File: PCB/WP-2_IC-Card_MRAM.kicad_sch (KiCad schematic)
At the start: 31 parts, among them J1 SMS-138-01-G-S, SW1 CUS-14TB, U1 MRxA08xxYSxxx, U2 MIC5317-3.3YD5, U3 4245, U4 4245, U5 4245, U6 4245

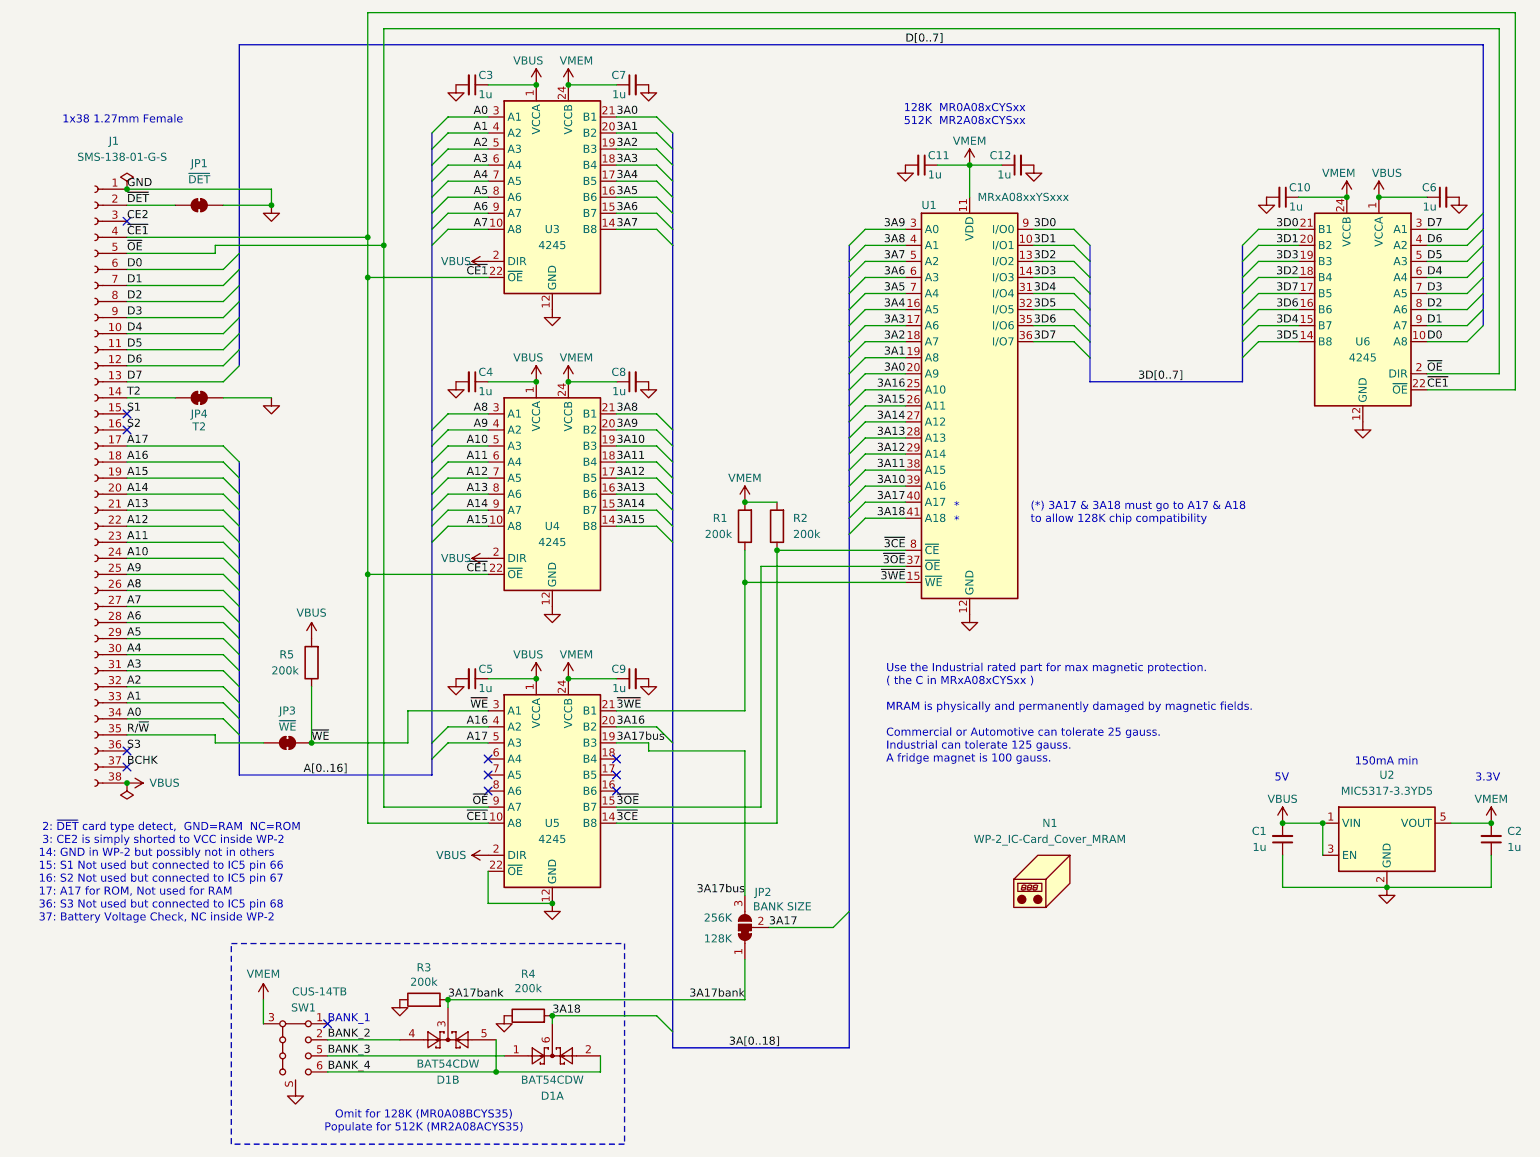
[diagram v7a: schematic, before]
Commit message: mram bav74 diodes
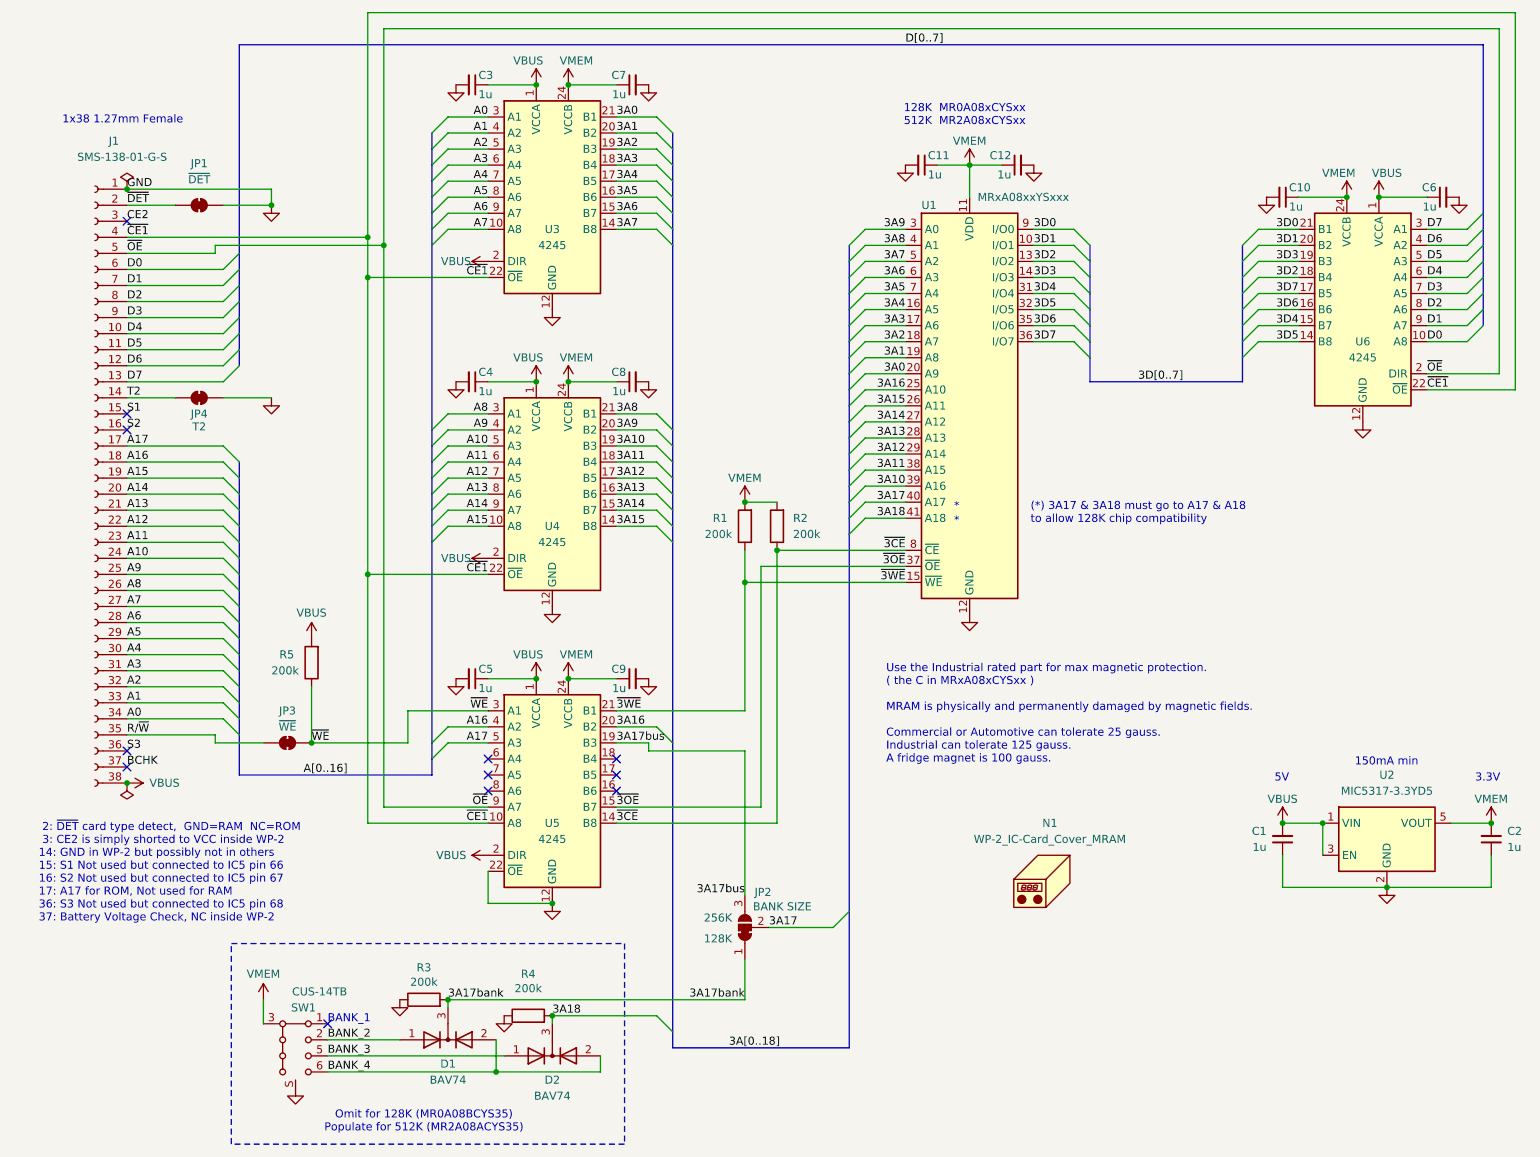
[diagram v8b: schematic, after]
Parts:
- removed D1: BAT54CDW, 000_LOCAL:TSSOP-6-symmetric, symbol 000_LOCAL:BAT54CDW
- added D1, D2: BAV74, 000_LOCAL:SOT-23, symbol 000_LOCAL:BAV170
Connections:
- net 3A17bank: now also D1.3 (K)
- net 3A18: now also D2.3 (K)
- net BANK_2: now also D1.1 (A)
- net BANK_3: now also D2.1 (A)
- net BANK_4: now also D1.2 (A), D2.2 (A)
